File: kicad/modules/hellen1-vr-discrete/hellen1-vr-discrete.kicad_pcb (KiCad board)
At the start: 4 copper layers, 15.2 x 9.8 mm, 45 parts, among them M750 Module-vr-discrete-0.2, U751 SRV05-4-P-T7, U752 74AHC1G02, U753 MCP6004, U754 MAX9142, U755 NC7SB3157P6X, U756 NC7SB3157P6X, U757 74AHC1G02

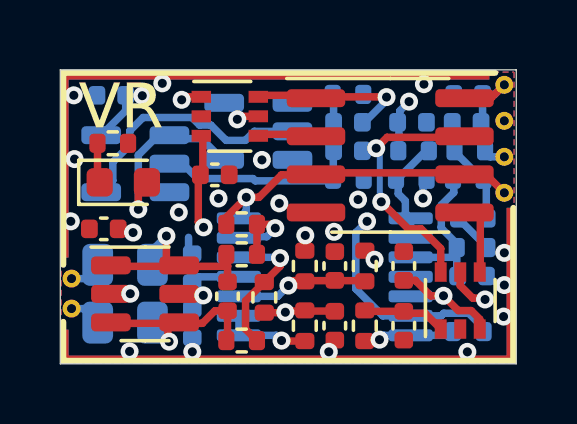
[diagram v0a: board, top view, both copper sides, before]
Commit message: ver 0.4
add C768, C769 (#247)
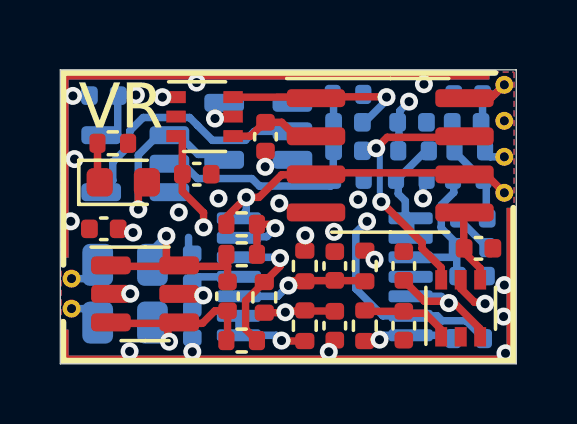
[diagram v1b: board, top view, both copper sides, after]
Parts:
- added C768: 10n, Capacitor_SMD:C_0402_1005Metric, F.Cu at (84.5, 87.5)
- added C769: 10n, Capacitor_SMD:C_0402_1005Metric, F.Cu at (91.6, 91.2)
- moved U755 0.84 mm to (82.5, 86.8)
- moved C765 0.60 mm to (82.2, 88.7)
- moved U756 0.26 mm to (91.0, 93.2)
- moved C761 0.25 mm to (79.2, 86.1)
- moved R763 0.24 mm to (91.3, 94.2)
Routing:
- net Net-(U754-Pad2): track 1.86 -> 3.10 mm
- net Net-(C756-Pad2): track 5.03 -> 5.85 mm
- net thresh_low: track 10.4 -> 11.0 mm
- net GND: track 1.98 -> 1.97 mm, vias 20 -> 19
